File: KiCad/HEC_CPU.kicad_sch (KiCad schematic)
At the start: 20 parts, among them J3 Conn_02x05_Odd_Even, J9 Conn_02x14_Odd_Even, SW2 SW_Push, U1 Z80CPU, U10 74LS32, U20 74LS574, U21 74LS574, U22 74LS02, U30 74LS74, U34 74LS393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

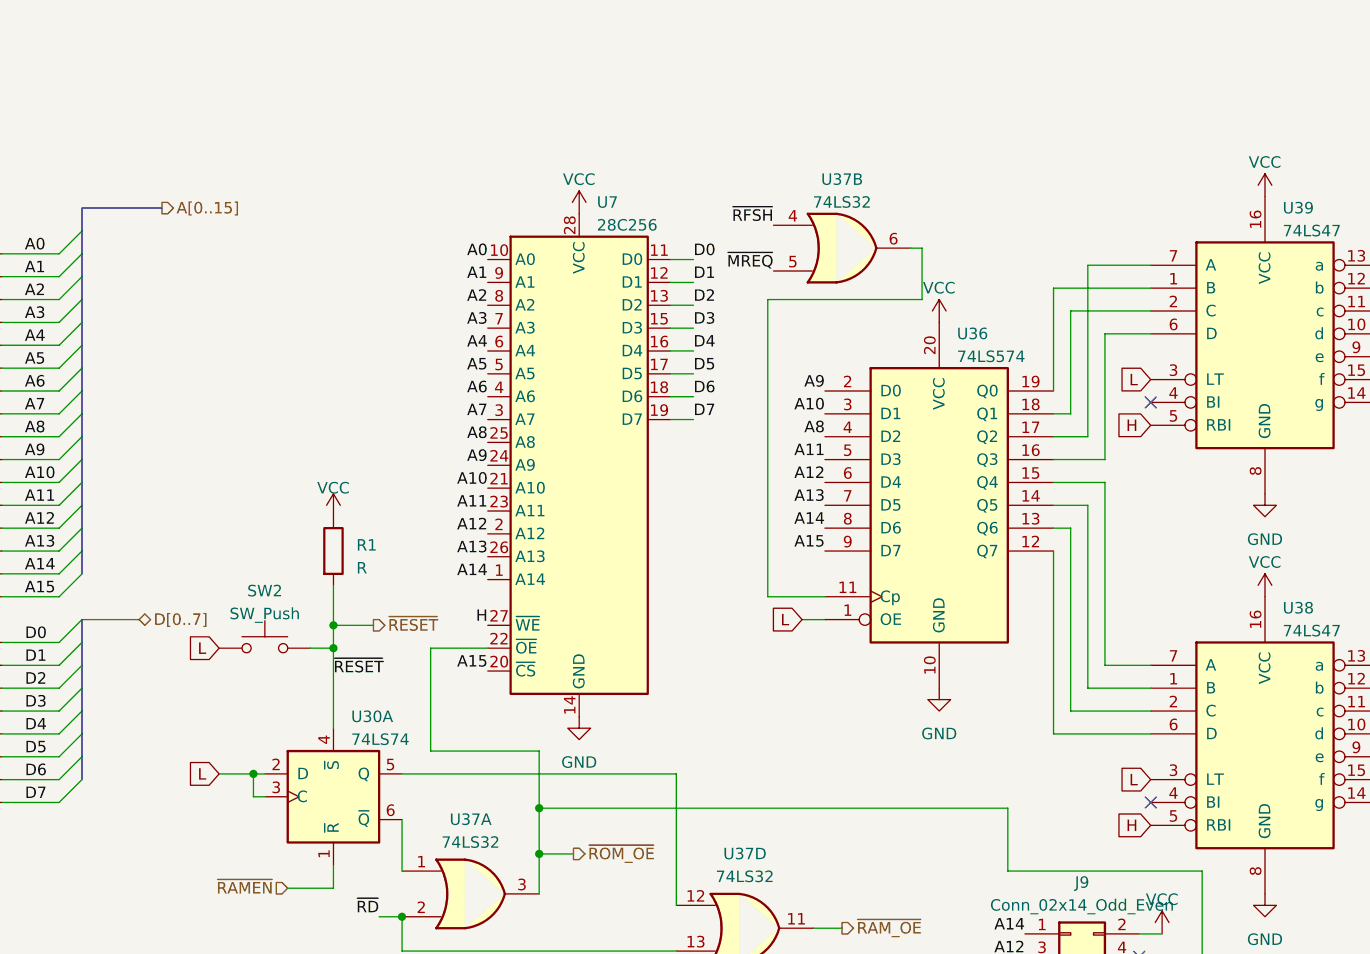
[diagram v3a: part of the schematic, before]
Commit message: Fixes to 2 issues found in the first prototype
Added jumper pads to allow user to switch between 74LS47 and DM9368 7-segment decoder chips, add reset timing capacitor.
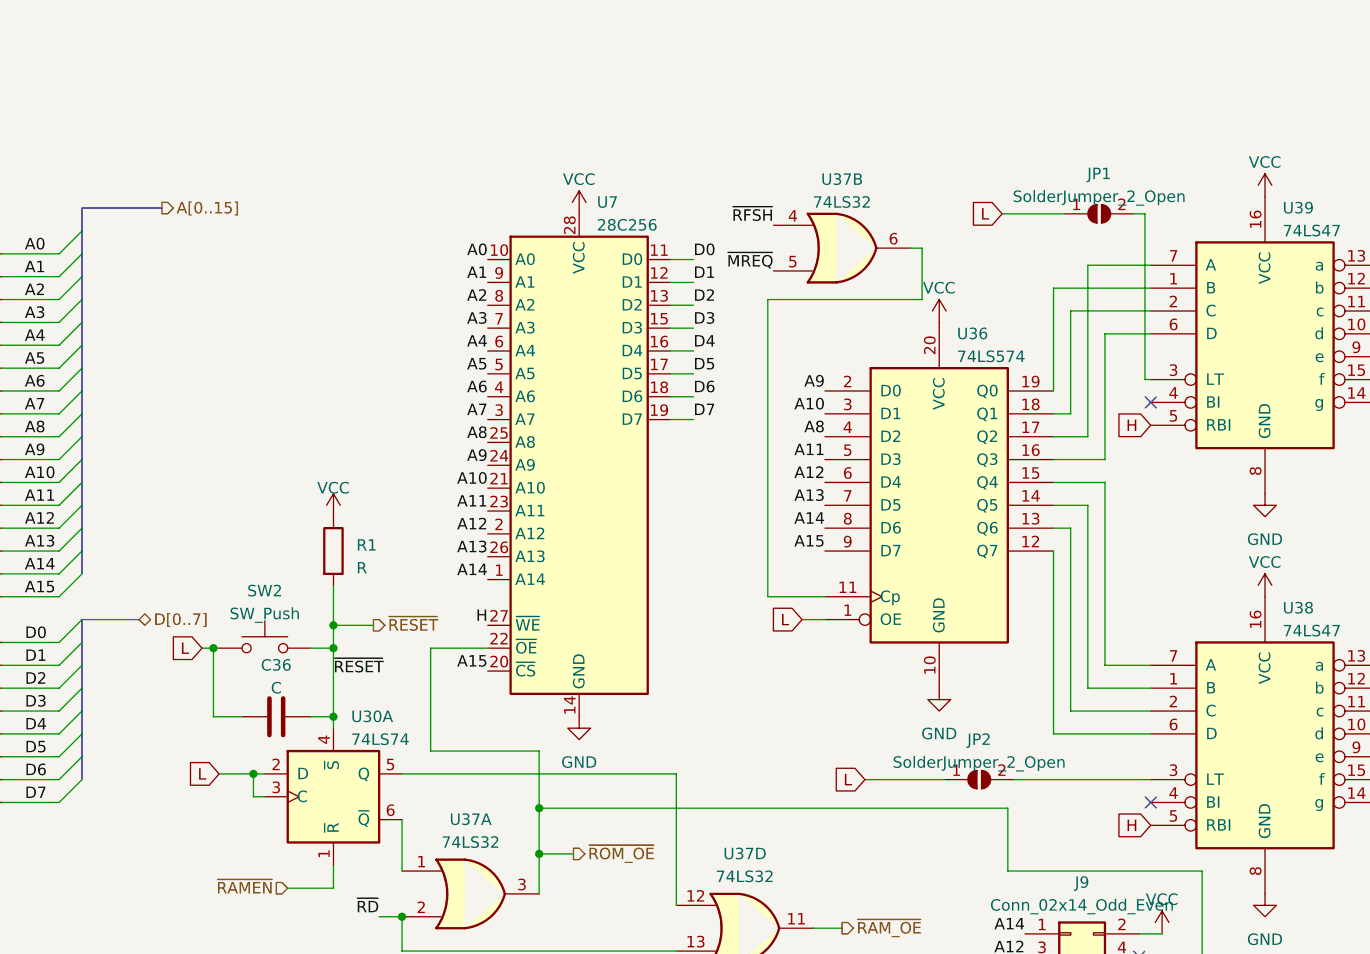
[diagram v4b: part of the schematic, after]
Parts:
- added C36: C, Capacitor_THT:C_Disc_D7.0mm_W2.5mm_P5.00mm, symbol Device:C
- added JP1, JP2: SolderJumper_2_Open, Jumper:SolderJumper-2_P1.3mm_Open_RoundedPad1.0x1.5mm, symbol Jumper:SolderJumper_2_Open
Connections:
- net L: now also C36.2, JP1.1 (A), JP2.1 (A); no longer U38.3 (LT), U39.3 (LT)
- net ~{RESET}: now also C36.1
- new net: JP2.2 (B), U38.3 (LT)
- new net: JP1.2 (B), U39.3 (LT)
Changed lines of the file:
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@@
   (junction (at 101.6 67.945) (diameter 0) (color 0 0 0 0)
   )
+  (junction (at 101.6 75.565) (diameter 0) (color 0 0 0 0)
+  )
   (junction (at 92.71 81.915) (diameter 0) (color 0 0 0 0)
   )
@@
   )
   (junction (at 245.11 137.795) (diameter 0) (color 0 0 0 0)
+  )
+  (junction (at 88.265 67.945) (diameter 0) (color 0 0 0 0)
   )
   (junction (at 105.41 172.72) (diameter 0) (color 0 0 0 0)
@@
     (stroke (width 0) (type default))
   )
+  (wire (pts (xy 88.265 75.565) (xy 88.265 67.945))
+    (stroke (width 0) (type default))
+  )
   (wire (pts (xy 245.11 137.795) (xy 248.92 137.795))
     (stroke (width 0) (type default))
@@
     (stroke (width 0) (type default))
   )
-  (wire (pts (xy 101.6 76.835) (xy 101.6 67.945))
+  (wire (pts (xy 101.6 76.835) (xy 101.6 75.565))
     (stroke (width 0) (type default))
   )
@@
     (stroke (width 0) (type default))
   )
+  (wire (pts (xy 86.995 67.945) (xy 88.265 67.945))
+    (stroke (width 0) (type default))
+  )
   (wire (pts (xy 242.57 43.18) (xy 242.57 53.34))
     (stroke (width 0) (type default))
@@
     (stroke (width 0) (type default))
   )
+  (wire (pts (xy 175.895 19.685) (xy 182.88 19.685))
+    (stroke (width 0) (type default))
+  )
   (wire (pts (xy 149.86 29.21) (xy 149.86 62.23))
     (stroke (width 0) (type default))
@@
     (stroke (width 0) (type default))
   )
+  (wire (pts (xy 177.165 82.55) (xy 192.405 82.55))
+    (stroke (width 0) (type default))
+  )
   (wire (pts (xy 237.49 53.34) (xy 242.57 53.34))
     (stroke (width 0) (type default))
@@
     (stroke (width 0) (type default))
   )
+  (wire (pts (xy 91.44 75.565) (xy 88.265 75.565))
+    (stroke (width 0) (type default))
+  )
   (wire (pts (xy 224.155 69.85) (xy 224.155 78.74))
     (stroke (width 0) (type default))
@@
     (stroke (width 0) (type default))
   )
+  (wire (pts (xy 88.265 67.945) (xy 88.9 67.945))
+    (stroke (width 0) (type default))
+  )
+  (wire (pts (xy 160.655 82.55) (xy 169.545 82.55))
+    (stroke (width 0) (type default))
+  )
   (wire (pts (xy 112.395 79.375) (xy 124.46 79.375))
     (stroke (width 0) (type default))
@@
     (stroke (width 0) (type default))
   )
+  (wire (pts (xy 191.77 38.1) (xy 192.405 38.1))
+    (stroke (width 0) (type default))
+  )
   (wire (pts (xy 20.32 74.93) (xy 29.21 74.93))
     (stroke (width 0) (type default))
@@
     (stroke (width 0) (type default))
   )
+  (wire (pts (xy 191.77 19.685) (xy 191.77 38.1))
+    (stroke (width 0) (type default))
+  )
   (wire (pts (xy 101.6 92.075) (xy 101.6 94.615))
     (stroke (width 0) (type default))
@@
     (stroke (width 0) (type default))
   )
+  (wire (pts (xy 99.06 75.565) (xy 101.6 75.565))
+    (stroke (width 0) (type default))
+  )
   (wire (pts (xy 38.735 121.92) (xy 38.735 126.365))
     (stroke (width 0) (type default))
   )
+  (wire (pts (xy 101.6 75.565) (xy 101.6 67.945))
+    (stroke (width 0) (type default))
+  )
   (wire (pts (xy 217.805 30.48) (xy 225.425 30.48))
     (stroke (width 0) (type default))
@@
   )
   (bus (pts (xy 73.66 34.29) (xy 73.66 31.75))
+    (stroke (width 0) (type default))
+  )
+  (wire (pts (xy 191.77 19.685) (xy 190.5 19.685))
     (stroke (width 0) (type default))
   )
@@
     (effects (font (size 1.27 1.27)) (justify right bottom))
   )
-  (global_label "L" (shape input) (at 88.9 67.945 180) (fields_autoplaced)
+  (global_label "L" (shape input) (at 86.995 67.945 180) (fields_autoplaced)
     (effects (font (size 1.27 1.27)) (justify right))
-    (property "Intersheetrefs" "${INTERSHEET_REFS}" (at 84.9661 67.945 0)
+    (property "Intersheetrefs" "${INTERSHEET_REFS}" (at 83.0611 67.945 0)
       (effects (font (size 1.27 1.27)) (justify right) hide)
     )
@@
     )
   )
-  (global_label "L" (shape input) (at 192.405 82.55 180) (fields_autoplaced)
+  (global_label "L" (shape input) (at 160.655 82.55 180) (fields_autoplaced)
     (effects (font (size 1.27 1.27)) (justify right))
-    (property "Intersheetrefs" "${INTERSHEET_REFS}" (at 188.4711 82.55 0)
+    (property "Intersheetrefs" "${INTERSHEET_REFS}" (at 156.7211 82.55 0)
       (effects (font (size 1.27 1.27)) (justify right) hide)
     )
   )
-  (global_label "L" (shape input) (at 192.405 38.1 180) (fields_autoplaced)
+  (global_label "L" (shape input) (at 175.895 19.685 180) (fields_autoplaced)
     (effects (font (size 1.27 1.27)) (justify right))
-    (property "Intersheetrefs" "${INTERSHEET_REFS}" (at 188.4711 38.1 0)
+    (property "Intersheetrefs" "${INTERSHEET_REFS}" (at 171.9611 19.685 0)
       (effects (font (size 1.27 1.27)) (justify right) hide)
     )
@@
         (path "/87935374-b60a-4f41-99da-94b76103dd77/73a0c68b-1e42-4c0d-ae31-b1a96d0648bb"
           (reference "#PWR027") (unit 1)
+        )
+      )
+    )
+  )
+  (symbol (lib_id "Jumper:SolderJumper_2_Open") (at 173.355 82.55 0) (unit 1)
+    (in_bom yes) (on_board yes) (dnp no) (fields_autoplaced)
+    (property "Reference" "JP2" (at 173.355 78.105 0)
+      (effects (font (size 1.27 1.27)))
+    )
+    (property "Value" "SolderJumper_2_Open" (at 173.355 80.645 0)
+      (effects (font (size 1.27 1.27)))
+    )
+    (property "Footprint" "Jumper:SolderJumper-2_P1.3mm_Open_RoundedPad1.0x1.5mm" (at 173.355 82.55 0)
+      (effects (font (size 1.27 1.27)) hide)
+    )
+    (property "Datasheet" "~" (at 173.355 82.55 0)
+      (effects (font (size 1.27 1.27)) hide)
+    )
+    (pin "1")
+    (pin "2")
+    (instances
+      (project "HEC1"
+        (path "/87935374-b60a-4f41-99da-94b76103dd77/73a0c68b-1e42-4c0d-ae31-b1a96d0648bb"
+          (reference "JP2") (unit 1)
         )
       )
@@
         (path "/87935374-b60a-4f41-99da-94b76103dd77/73a0c68b-1e42-4c0d-ae31-b1a96d0648bb"
           (reference "#PWR096") (unit 1)
+        )
+      )
+    )
+  )
+  (symbol (lib_id "Device:C") (at 95.25 75.565 270) (unit 1)
+    (in_bom yes) (on_board yes) (dnp no) (fields_autoplaced)
+    (property "Reference" "C36" (at 95.25 69.85 90)
+      (effects (font (size 1.27 1.27)))
+    )
+    (property "Value" "C" (at 95.25 72.39 90)
+      (effects (font (size 1.27 1.27)))
+    )
+    (property "Footprint" "Capacitor_THT:C_Disc_D7.0mm_W2.5mm_P5.00mm" (at 91.44 76.5302 0)
+      (effects (font (size 1.27 1.27)) hide)
+    )
+    (property "Datasheet" "~" (at 95.25 75.565 0)
+      (effects (font (size 1.27 1.27)) hide)
+    )
+    (pin "1")
+    (pin "2")
+    (instances
+      (project "HEC1"
+        (path "/87935374-b60a-4f41-99da-94b76103dd77/73a0c68b-1e42-4c0d-ae31-b1a96d0648bb"
+          (reference "C36") (unit 1)
         )
       )
@@
         )
       )
+    )
+  )
+  (symbol (lib_id "Jumper:SolderJumper_2_Open") (at 186.69 19.685 0) (unit 1)
+    (in_bom yes) (on_board yes) (dnp no) (fields_autoplaced)
+    (property "Reference" "JP1" (at 186.69 15.24 0)
+      (effects (font (size 1.27 1.27)))
+    )
+    (property "Value" "SolderJumper_2_Open" (at 186.69 17.78 0)
+      (effects (font (size 1.27 1.27)))
+    )
+    (property "Footprint" "Jumper:SolderJumper-2_P1.3mm_Open_RoundedPad1.0x1.5mm" (at 186.69 19.685 0)
+      (effects (font (size 1.27 1.27)) hide)
+    )
+    (property "Datasheet" "~" (at 186.69 19.685 0)
+      (effects (font (size 1.27 1.27)) hide)
+    )
+    (pin "1")
+    (pin "2")
+    (instances
+      (project "HEC1"
+        (path "/87935374-b60a-4f41-99da-94b76103dd77/73a0c68b-1e42-4c0d-ae31-b1a96d0648bb"
+          (reference "JP1") (unit 1)
+        )
+      )

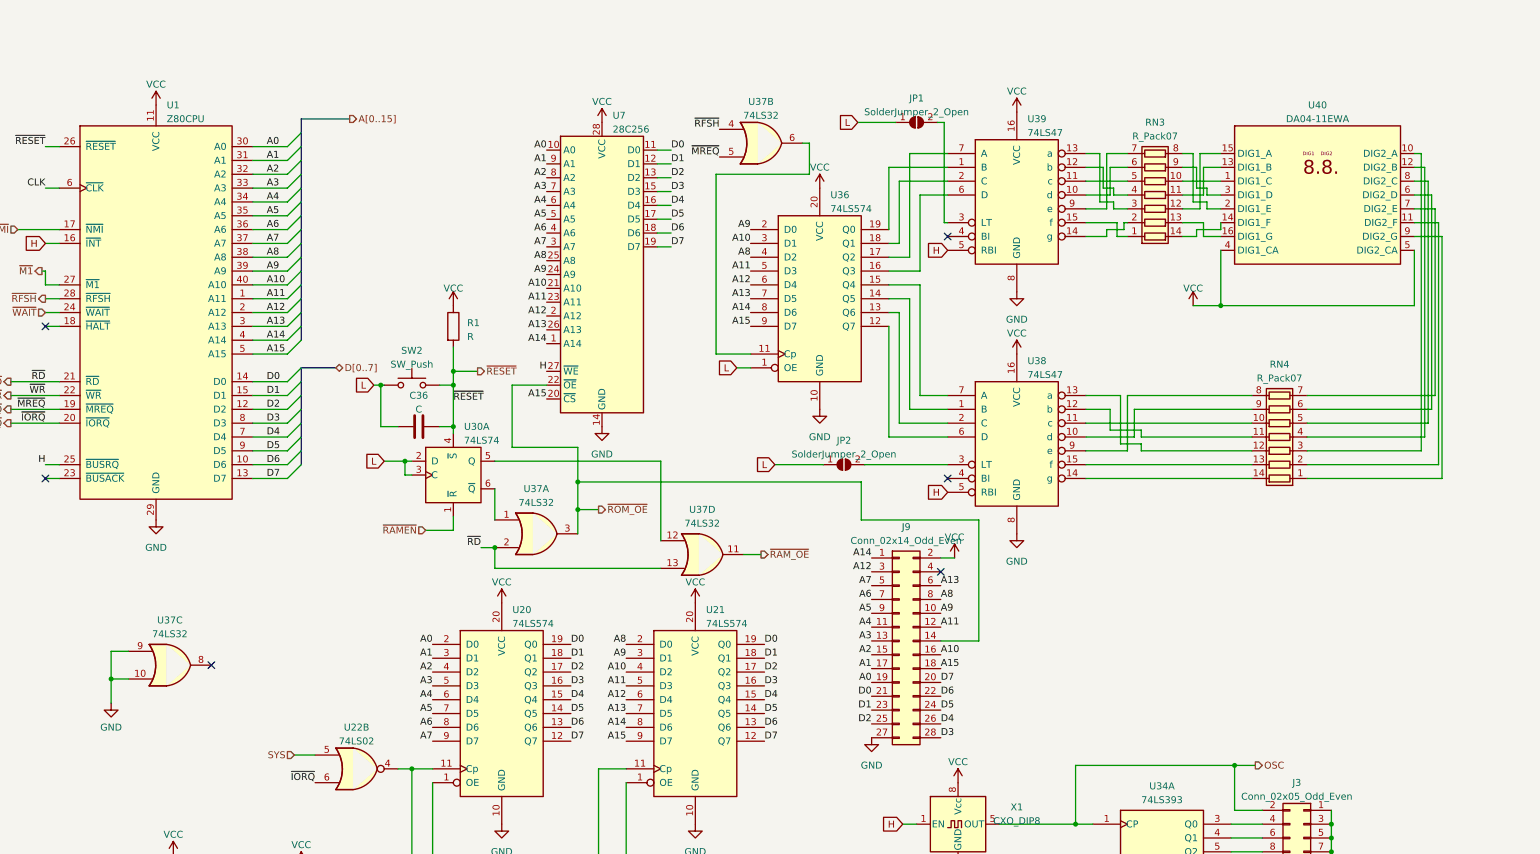
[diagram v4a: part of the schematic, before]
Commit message: Change LED display type
Changed LED display to include two decimal points to indicate usr/sys mode. This type of LED display is easier to source.
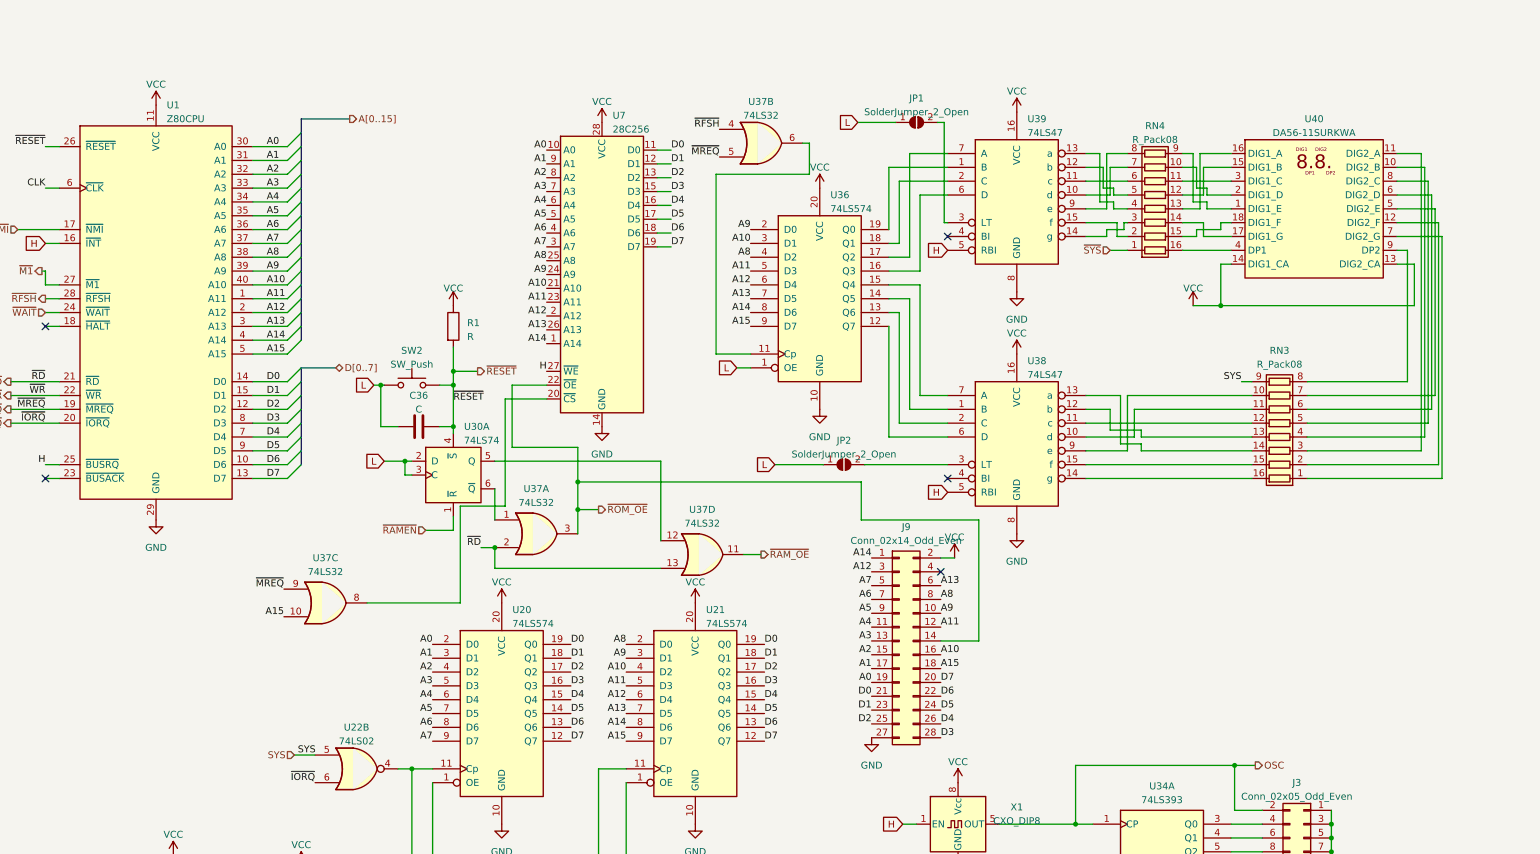
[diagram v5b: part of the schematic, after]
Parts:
- removed RN3, RN4: R_Pack07, Package_DIP:DIP-14_W7.62mm, symbol Device:R_Pack07
- removed U40: DA04-11EWA, Display_7Segment:DA04-11SURKWA, symbol Display_Character:DA04-11EWA
- added RN3, RN4: R_Pack08, symbol Device:R_Pack08
- added U40: DA56-11SURKWA, Display_7Segment:DA56-11SURKWA, symbol Display_Character:DA56-11SURKWA
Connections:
- net A15: now also U37.10; no longer U7.20 (~{CS})
- net GND: no longer U37.10, U37.9
- net SYS: now also RN3.9 (R8.2)
- net VCC: now also U40.13 (DIG2_CA), U40.14 (DIG1_CA)
- net ~{MREQ}: now also U37.9
- net at U38.11 (c): now also RN3.12 (R5.2)
- net at U38.12 (b): now also RN3.13 (R4.2)
- net at U38.13 (a): now also RN3.14 (R3.2)
- net at U38.15 (f): now also RN3.15 (R2.2)
- net at U38.14 (g): now also RN3.16 (R1.2)
- net at U38.9 (e): now also RN3.10 (R7.2)
- net at U38.10 (d): now also RN3.11 (R6.2)
- net at U37.8: now also U7.20 (~{CS})
- net at U39.15 (f): now also RN4.2 (R2.1)
- net at U39.14 (g): now also RN4.3 (R3.1)
- net at U39.13 (a): now also RN4.4 (R4.1)
- net at U39.12 (b): now also RN4.5 (R5.1)
- net at U39.11 (c): now also RN4.6 (R6.1)
- net at U39.10 (d): now also RN4.7 (R7.1)
- net at U39.9 (e): now also RN4.8 (R8.1)
- new net: RN4.10 (R7.2), U40.2 (DIG1_D)
- new net: RN4.11 (R6.2), U40.3 (DIG1_C)
- new net: RN4.12 (R5.2), U40.15 (DIG1_B)
- new net: RN4.13 (R4.2), U40.16 (DIG1_A)
- new net: RN4.14 (R3.2), U40.17 (DIG1_G)
- new net: RN4.15 (R2.2), U40.18 (DIG1_F)
- new net: RN4.16 (R1.2), U40.4 (DP1)
- new net: RN4.9 (R8.2), U40.1 (DIG1_E)
- new net: RN3.1 (R1.1), U40.7 (DIG2_G)
- new net: RN3.2 (R2.1), U40.12 (DIG2_F)
- new net: RN3.3 (R3.1), U40.11 (DIG2_A)
- new net: RN3.4 (R4.1), U40.10 (DIG2_B)
- new net: RN3.5 (R5.1), U40.8 (DIG2_C)
- new net: RN3.6 (R6.1), U40.6 (DIG2_D)
- new net: RN3.7 (R7.1), U40.5 (DIG2_E)
- new net: RN3.8 (R8.1), U40.9 (DP2)
- new net ~{SYS}: RN4.1 (R1.1)
- no-connect marks 6 -> 5
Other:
- moved on the sheet: U37C
